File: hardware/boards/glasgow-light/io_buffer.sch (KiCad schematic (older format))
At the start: 75 parts, among them J2 IDC-Header_2x5_P2.54mm, J3 IDC-Header_2x5_P2.54mm, U11 TPS73101DBV, U12 INA180A2, U16 SN74LVC1T45DCKR, U17 SN74LVC1T45DCKR, U18 SN74LVC1T45DCKR, U19 PCA6408APW, U19 SN74LVC1T45DCKR, U20 SN74LVC1T45DCKR, U21 SN74LVC1T45DCKR, U5 SN74LVC1T45DCKR, U6 SN74LVC1T45DCKR

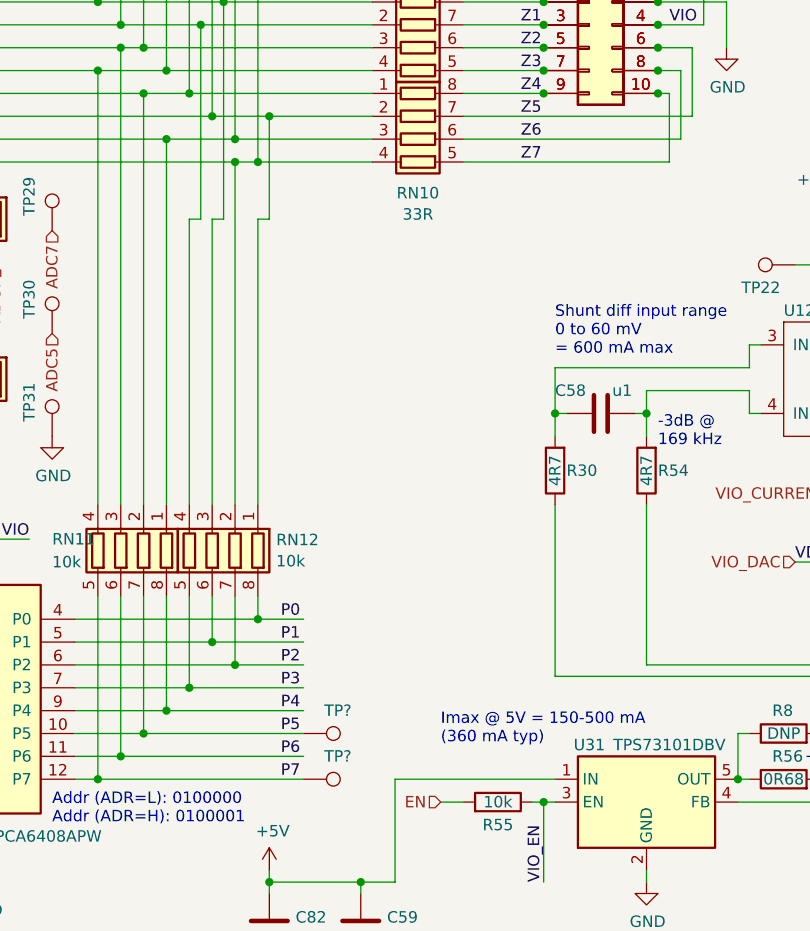
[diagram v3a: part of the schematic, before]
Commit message: add LEDs for VIO and Y7
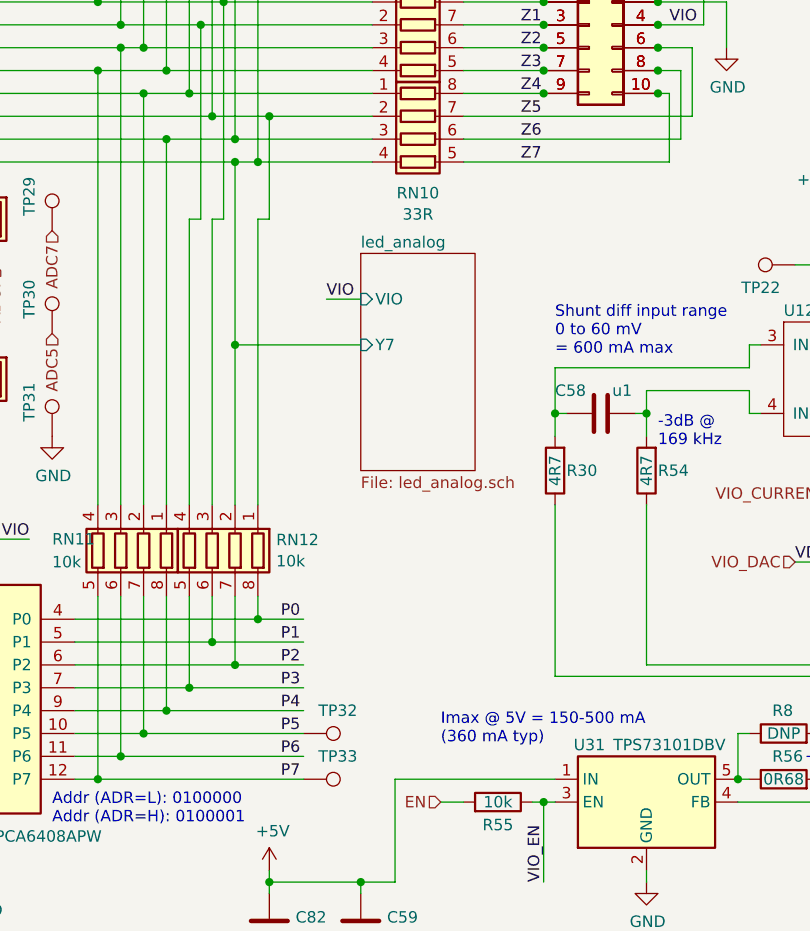
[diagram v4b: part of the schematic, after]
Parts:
- gave numbers to parts that had none: 2
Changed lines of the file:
@@
 $Descr A4 11693 8268
 encoding utf-8
-Sheet 3 3
+Sheet 3 4
 Title "I/O Buffer"
 Date ""
@@
 	7750 2750 7850 2750
 Wire Wire Line
-	7750 2750 7750 4250
+	7750 2750 7750 3550
 Wire Wire Line
 	1650 2500 1650 4650
@@
 P 8050 5250
 AR Path="/604DF2C1" Ref="TP?"  Part="1"
-AR Path="/5C7B59B0/5C9E337E/604DF2C1" Ref="TP?"  Part="1"
+AR Path="/5C7B59B0/5C9E337E/604DF2C1" Ref="TP32"  Part="1"
 AR Path="/5C7B59B0/5C9E338E/604DF2C1" Ref="TP?"  Part="1"
 AR Path="/5FFD4B90/604DF2C1" Ref="TP?"  Part="1"
 AR Path="/5FFD4BA1/604DF2C1" Ref="TP?"  Part="1"
-F 0 "TP?" V 7950 5400 50  0000 C CNN
+F 0 "TP32" V 7950 5400 50  0000 C CNN
 F 1 "P5" V 8154 5324 50  0001 C CNN
 F 2 "TestPoint:TestPoint_Pad_D1.0mm" H 8250 5250 50  0001 C CNN
@@
 P 8050 5450
 AR Path="/604E0486" Ref="TP?"  Part="1"
-AR Path="/5C7B59B0/5C9E337E/604E0486" Ref="TP?"  Part="1"
+AR Path="/5C7B59B0/5C9E337E/604E0486" Ref="TP33"  Part="1"
 AR Path="/5C7B59B0/5C9E338E/604E0486" Ref="TP?"  Part="1"
 AR Path="/5FFD4B90/604E0486" Ref="TP?"  Part="1"
 AR Path="/5FFD4BA1/604E0486" Ref="TP?"  Part="1"
-F 0 "TP?" V 7950 5600 50  0000 C CNN
+F 0 "TP33" V 7950 5600 50  0000 C CNN
 F 1 "P7" V 8154 5524 50  0001 C CNN
 F 2 "TestPoint:TestPoint_Pad_D1.0mm" H 8250 5450 50  0001 C CNN
@@
 	0    1    1    0
 $EndComp
+$Sheet
+S 8300 3150 500  950
+U 60515668
+F0 "led_analog" 50
+F1 "led_analog.sch" 50
+F2 "VIO" I L 8300 3350 50
+F3 "Y7" I L 8300 3550 50
+$EndSheet
+Text Label 8150 3350 0    50   ~ 0
+VIO
+Wire Wire Line
+	8150 3350 8300 3350
+Connection ~ 7750 3550
+Wire Wire Line
+	7750 3550 7750 4250
+Wire Wire Line
+	7750 3550 8300 3550
 $EndSCHEMATC

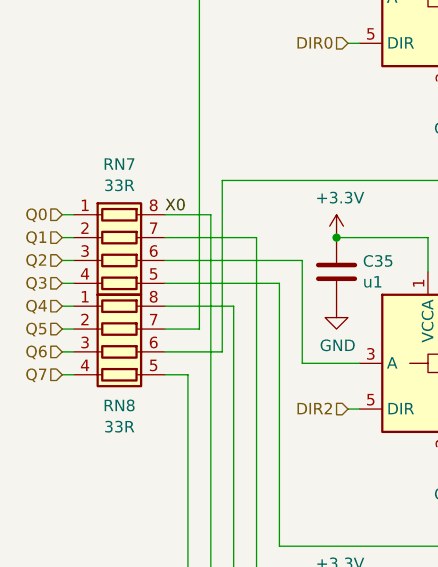
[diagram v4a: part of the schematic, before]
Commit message: start routing FPGA
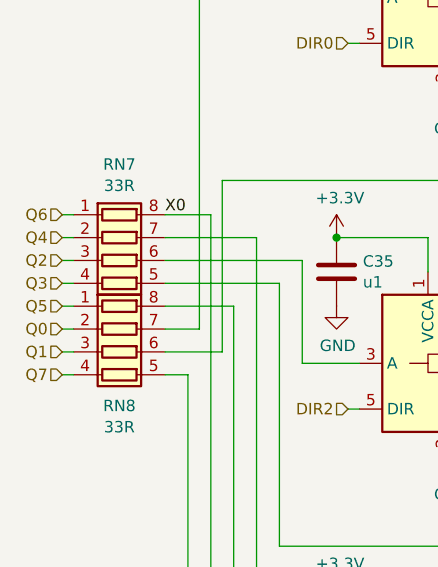
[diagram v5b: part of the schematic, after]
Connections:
- net Q0: now also RN2.2 (R2.1); no longer RN1.1 (R1.1)
- net Q1: now also RN2.3 (R3.1); no longer RN1.2 (R2.1)
- net Q4: now also RN1.2 (R2.1); no longer RN2.1 (R1.1)
- net Q5: now also RN2.1 (R1.1); no longer RN2.2 (R2.1)
- net Q6: now also RN1.1 (R1.1); no longer RN2.3 (R3.1)
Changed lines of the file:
@@
 	2050 1650 2100 1650
 Text HLabel 800  2400 0    50   Input ~ 0
-Q0
+Q6
 Text HLabel 2050 1650 0    50   Input ~ 0
 DIR0
@@
 	2050 4850 2100 4850
 Text HLabel 800  2800 0    50   Input ~ 0
-Q4
+Q5
 Text HLabel 2050 4850 0    50   Input ~ 0
 DIR4
@@
 	2050 6450 2100 6450
 Text HLabel 800  3000 0    50   Input ~ 0
-Q6
+Q1
 Text HLabel 2050 6450 0    50   Input ~ 0
 DIR6
@@
 	3800 2450 3850 2450
 Text HLabel 800  2500 0    50   Input ~ 0
-Q1
+Q4
 Text HLabel 3800 2450 0    50   Input ~ 0
 DIR1
@@
 	3800 5650 3850 5650
 Text HLabel 800  2900 0    50   Input ~ 0
-Q5
+Q0
 Text HLabel 3800 5650 0    50   Input ~ 0
 DIR5
